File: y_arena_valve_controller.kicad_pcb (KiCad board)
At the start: 2 copper layers, 74.9 x 97.8 mm, 20 parts, among them P1 PWR_JACK_2.1x5.5_SMD_VERT

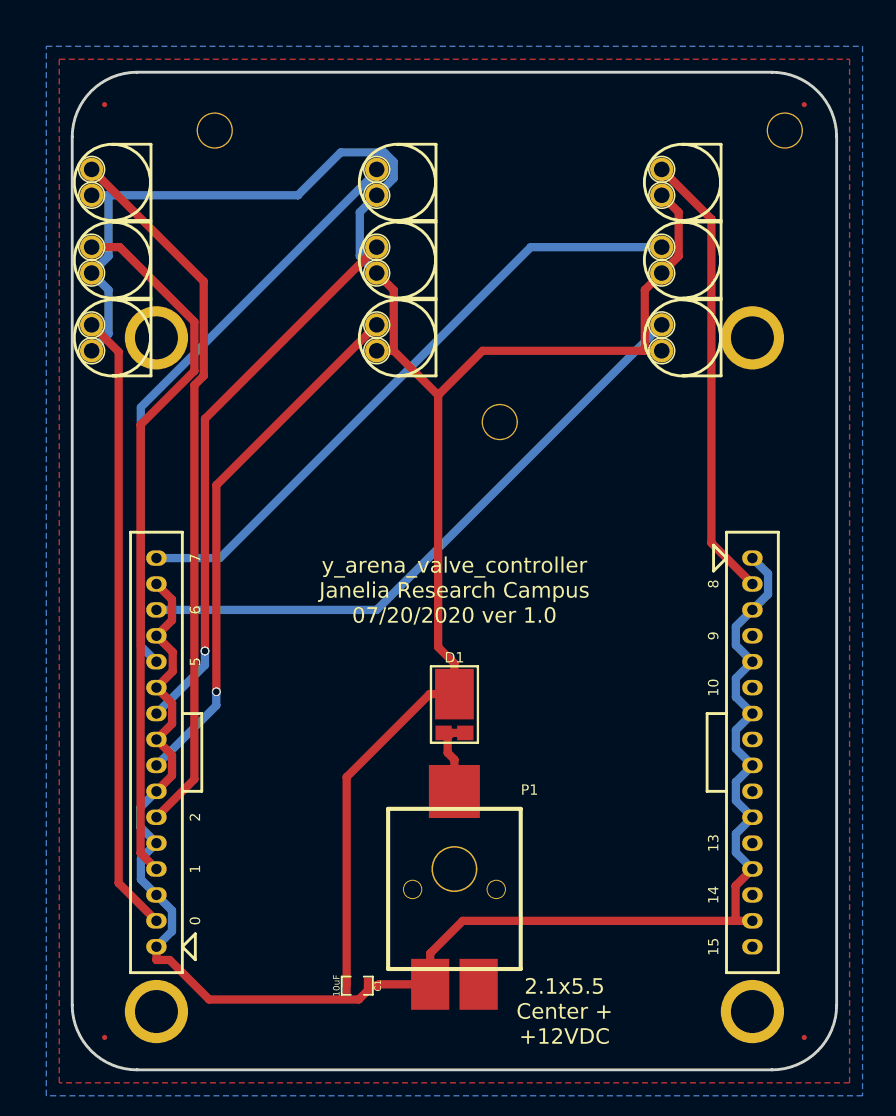
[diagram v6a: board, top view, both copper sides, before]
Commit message: Progress towards v1.1
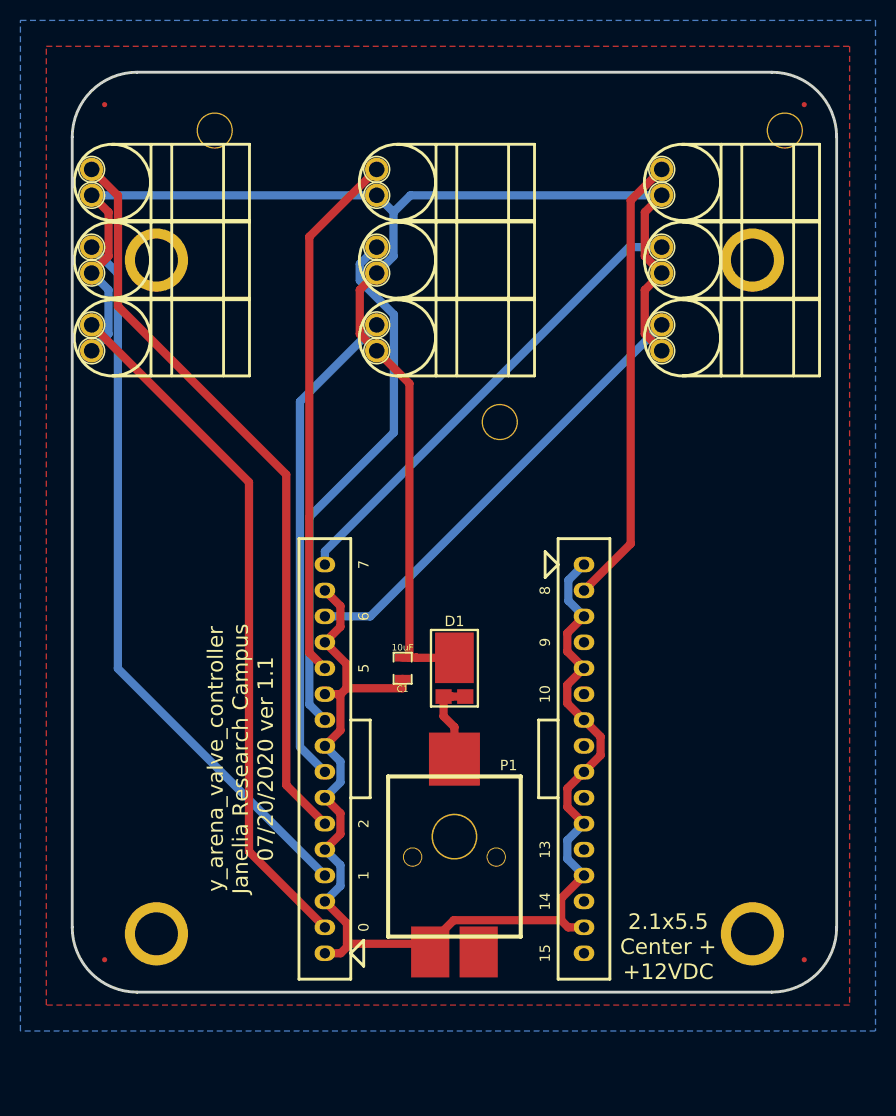
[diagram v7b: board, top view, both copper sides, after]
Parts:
- moved C1 31.4 mm to (83.2, 109.2), turned to 0 degrees
- moved FID3 7.62 mm to (122.6, 137.8)
- moved FID4 7.62 mm to (54.0, 137.8)
- moved PHIDGET1 7.62 mm to (88.3, 102.2)
- moved D1 3.56 mm to (88.3, 109.2)
- moved P1 3.17 mm to (88.3, 125.7)
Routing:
- net VCC: track 183.5 -> 145.4 mm
- net GND: track 155.5 -> 122.1 mm
- net /VALVE_6: track 61.1 -> 44.9 mm
- net /VALVE_7: track 62.2 -> 46.7 mm
- net /VALVE_0: track 61.1 -> 68.5 mm
- net /VALVE_5: track 58.5 -> 52.3 mm
- net /VALVE_3: track 52.1 -> 47.9 mm, vias 1 -> 0
- net /VALVE_2: track 70.0 -> 73.6 mm
- net /VALVE_4: track 54.7 -> 52.5 mm, vias 1 -> 0
- net /VALVE_1: track 69.6 -> 71.1 mm
- net VAA: track 8.08 -> 8.70 mm
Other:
- board size 74.9 x 97.8 mm -> 74.9 x 90.2 mm
- board text added: "y_arena_valve_controller Janelia Research Campus 07/20/2020 ver 1.1"
- board text removed: "y_arena_valve_controller Janelia Research Campus 07/20/2020 ver 1.0"

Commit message: Finished v1.1
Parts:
- S1, S2, S3, S4, S5, S6, S7, S8, S9: footprint valve:LEECO_LHDB -> y_arena_valve_controller:LEECO_LHDB
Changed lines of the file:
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@@
       (net 11 GND))
   )
-  (module valve:LEECO_LHDB (layer F.Cu)
+  (module y_arena_valve_controller:LEECO_LHDB (layer F.Cu)
     (at 52.705 76.835 90)
     (fp_text reference S1 (at -4.445 0 180) (layer B.SilkS)
@@
       (net 12 VCC))
   )
-  (module valve:LEECO_LHDB (layer F.Cu)
+  (module y_arena_valve_controller:LEECO_LHDB (layer F.Cu)
     (at 52.705 69.215 90)
     (fp_text reference S2 (at 0 6.985 90) (layer B.SilkS)
@@
       (net 12 VCC))
   )
-  (module valve:LEECO_LHDB (layer F.Cu)
+  (module y_arena_valve_controller:LEECO_LHDB (layer F.Cu)
     (at 52.705 61.595 90)
     (fp_text reference S3 (at 0 6.985 270) (layer B.SilkS)
@@
       (net 12 VCC))
   )
-  (module valve:LEECO_LHDB (layer F.Cu)
+  (module y_arena_valve_controller:LEECO_LHDB (layer F.Cu)
     (at 80.645 76.835 90)
     (fp_text reference S4 (at 0 6.985 90) (layer B.SilkS)
@@
       (net 12 VCC))
   )
-  (module valve:LEECO_LHDB (layer F.Cu)
+  (module y_arena_valve_controller:LEECO_LHDB (layer F.Cu)
     (at 80.645 69.215 90)
     (fp_text reference S5 (at 0 6.985 90) (layer B.SilkS)
@@
       (net 12 VCC))
   )
-  (module valve:LEECO_LHDB (layer F.Cu)
+  (module y_arena_valve_controller:LEECO_LHDB (layer F.Cu)
     (at 80.645 61.595 90)
     (fp_text reference S6 (at 0 6.985 90) (layer B.SilkS)
@@
       (net 12 VCC))
   )
-  (module valve:LEECO_LHDB (layer F.Cu)
+  (module y_arena_valve_controller:LEECO_LHDB (layer F.Cu)
     (at 108.585 76.835 90)
     (fp_text reference S7 (at -4.445 0 180) (layer B.SilkS)
@@
       (net 12 VCC))
   )
-  (module valve:LEECO_LHDB (layer F.Cu)
+  (module y_arena_valve_controller:LEECO_LHDB (layer F.Cu)
     (at 108.585 69.215 90)
     (fp_text reference S8 (at 0 6.985 90) (layer B.SilkS)
@@
       (net 12 VCC))
   )
-  (module valve:LEECO_LHDB (layer F.Cu)
+  (module y_arena_valve_controller:LEECO_LHDB (layer F.Cu)
     (at 108.585 61.595 90)
     (fp_text reference S9 (at 0 6.985 270) (layer B.SilkS)
